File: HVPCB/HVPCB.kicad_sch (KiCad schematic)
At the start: 48 parts, among them U1 NE555DR_C695838, U10 Micro Fit 2P, U2 SN74LVC1GU04DBVR, U3 B0505S-2WR2, U4 LM392MX, U5 AO3400A, U6 AO3400A, U7 KT-0603R, U8 KT-0603R, U9 KT-0603R

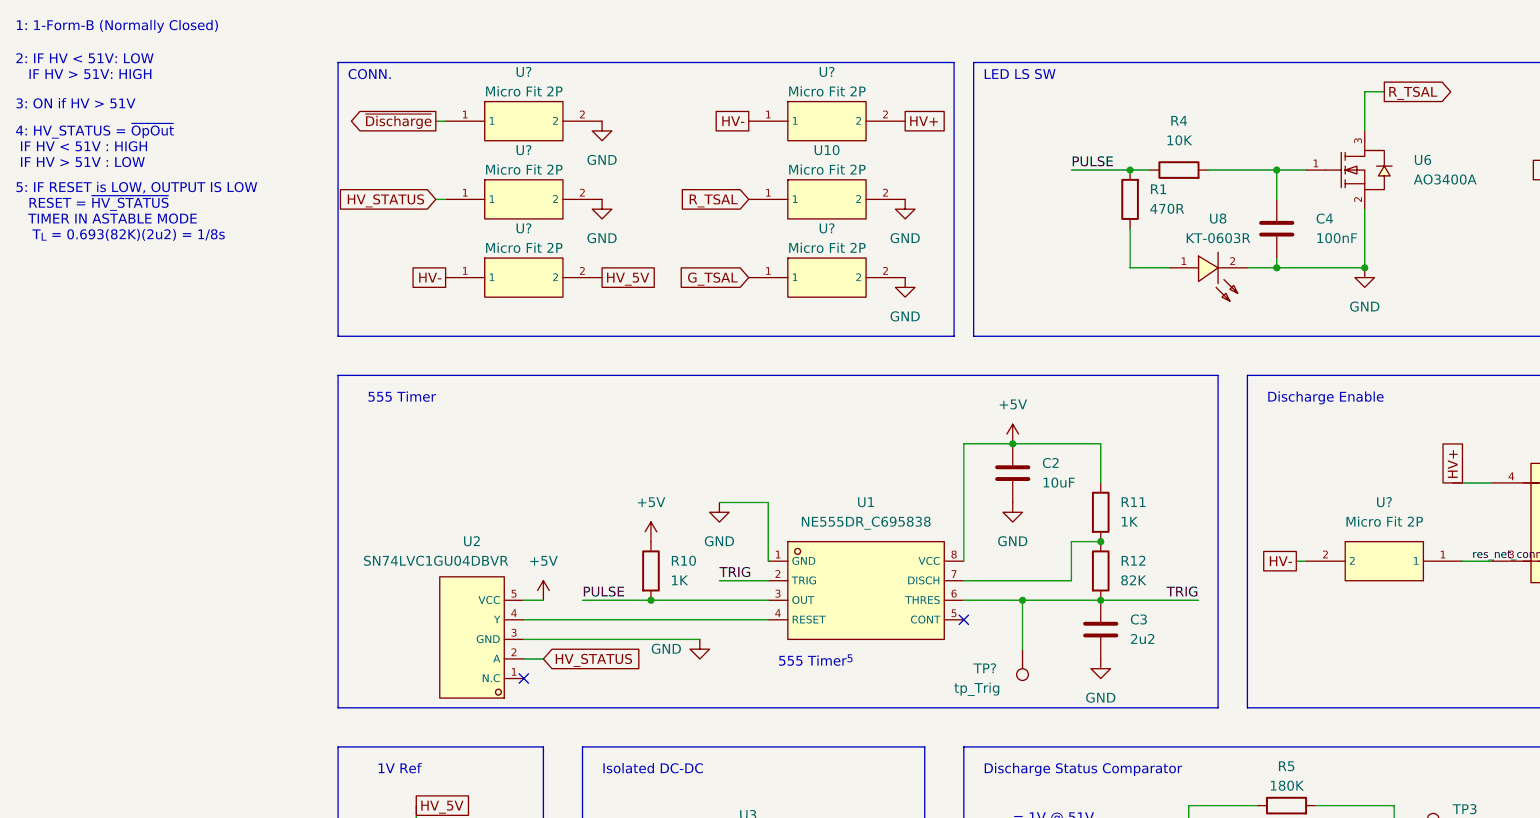
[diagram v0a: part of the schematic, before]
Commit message: updated board drawing to add mounting holes, updated test points and moved components to general proximity
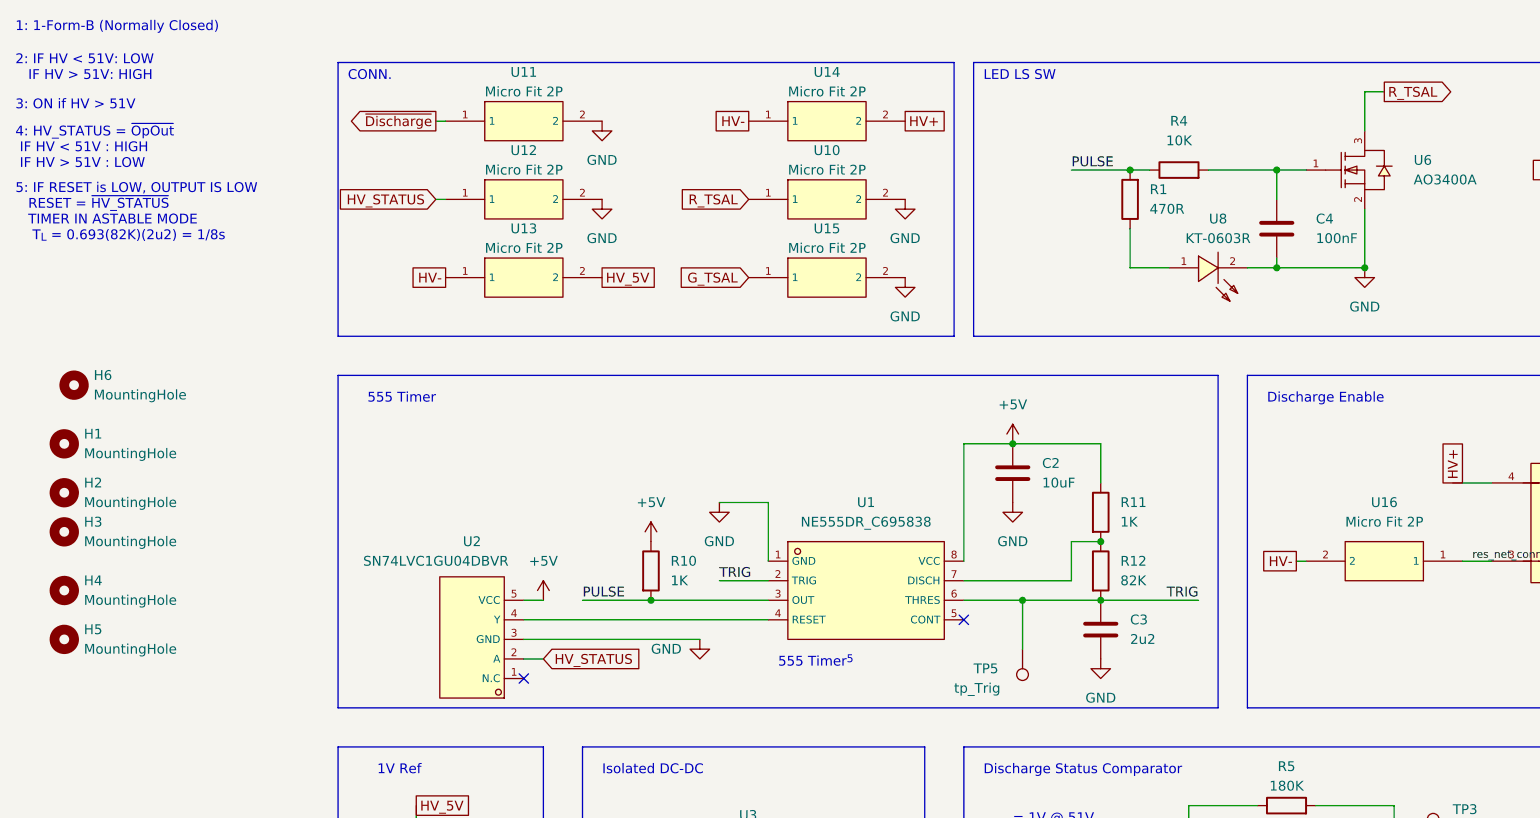
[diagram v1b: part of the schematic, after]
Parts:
- added H1, H2, H3, H4, H5, H6: MountingHole, MountingHole:MountingHole_2.2mm_M2, symbol Mechanical:MountingHole
- TP1: footprint TestPoint:TestPoint_Pad_D2.0mm -> TestPoint:TestPoint_THTPad_D2.0mm_Drill1.0mm
- TP2, TP3, TP4: footprint (none) -> TestPoint:TestPoint_THTPad_D2.0mm_Drill1.0mm
- TP5: renamed from TP?; footprint TestPoint:TestPoint_Pad_D2.0mm -> TestPoint:TestPoint_THTPad_D2.0mm_Drill1.0mm
- gave numbers to parts that had none: 6

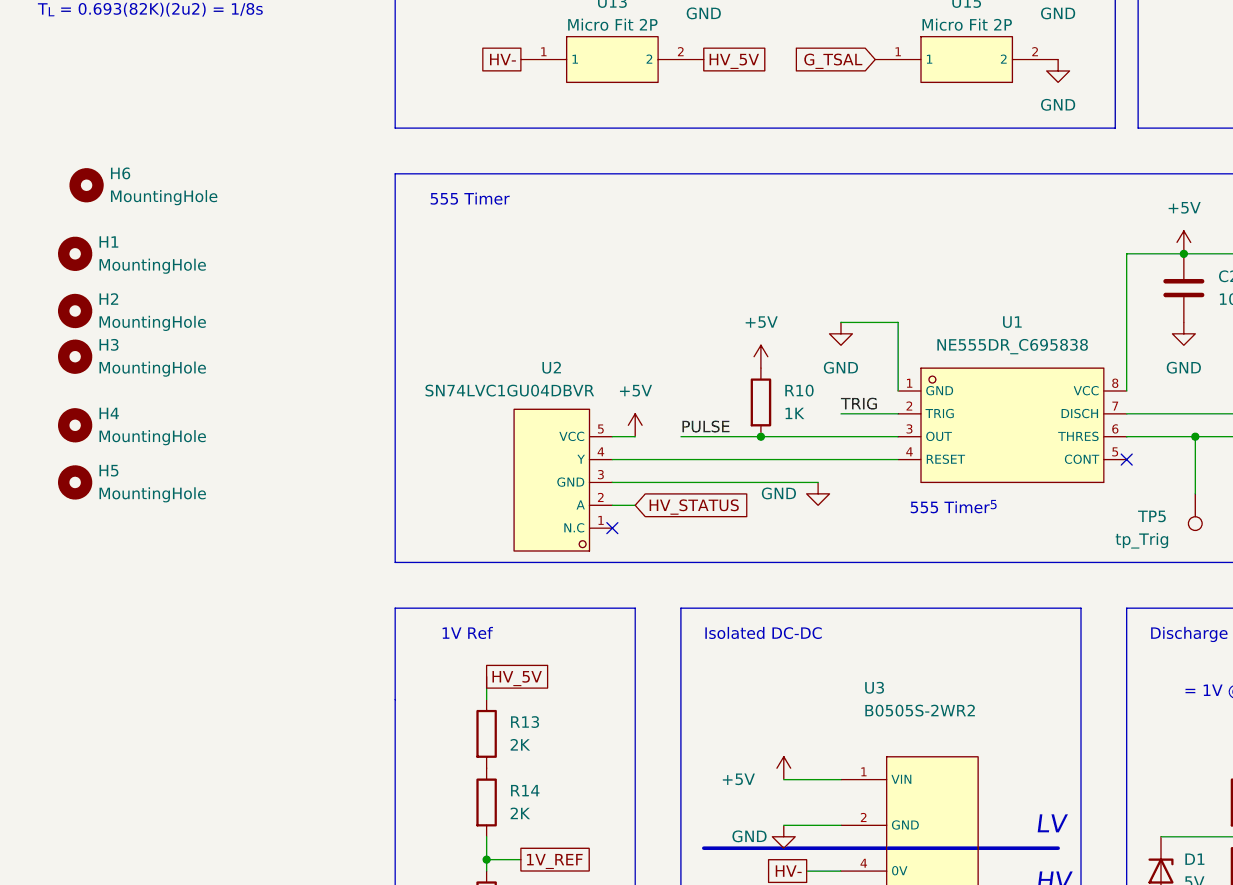
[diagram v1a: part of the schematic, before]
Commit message: added mounting holes and organized board
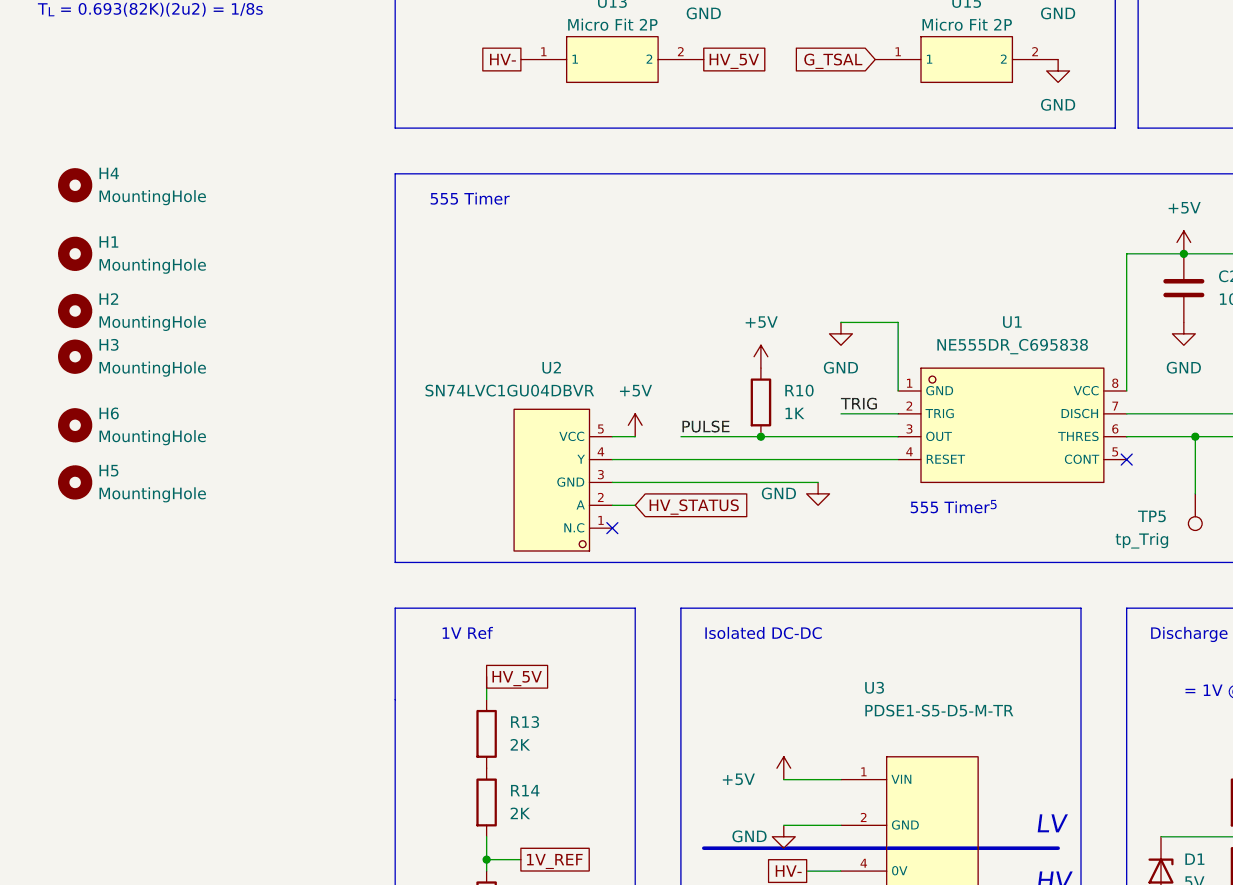
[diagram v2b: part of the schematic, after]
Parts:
- U3: value B0505S-2WR2 -> PDSE1-S5-D5-M-TR; footprint footprint:PWRM-TH_BXXXXS-2WR2 -> Converter_DCDC:CUI Isolated DC-DC; LCSC C41613 -> Mouser; Supplier Link https://www.lcsc.com/product-detail/Power-Modules_B0505S-2W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 -> https://www.mouser.com/ProductDetail/CUI-Inc/PDSE1-S5-D5-M-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
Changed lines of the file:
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@@
     (pin "1")
+  )
+  (symbol (lib_id "Mechanical:MountingHole") (at 22.86 91.44 0) (unit 1)
+    (in_bom yes) (on_board yes) (fields_autoplaced)
+    (property "Reference" "H6" (id 0) (at 25.4 90.1699 0)
+      (effects (font (size 1.27 1.27)) (justify left))
+    )
+    (property "Value" "MountingHole" (id 1) (at 25.4 92.7099 0)
+      (effects (font (size 1.27 1.27)) (justify left))
+    )
+    (property "Footprint" "MountingHole:MountingHole_2.2mm_M2" (id 2) (at 22.86 91.44 0)
+      (effects (font (size 1.27 1.27)) hide)
+    )
+    (property "Datasheet" "~" (id 3) (at 22.86 91.44 0)
+      (effects (font (size 1.27 1.27)) hide)
+    )
   )
   (symbol (lib_id "power:GND") (at 248.92 152.4 0) (unit 1)
@@
     (pin "1")
   )
-  (symbol (lib_id "Mechanical:MountingHole") (at 22.86 91.44 0) (unit 1)
-    (in_bom yes) (on_board yes) (fields_autoplaced)
-    (property "Reference" "H4" (id 0) (at 25.4 90.1699 0)
-      (effects (font (size 1.27 1.27)) (justify left))
-    )
-    (property "Value" "MountingHole" (id 1) (at 25.4 92.7099 0)
-      (effects (font (size 1.27 1.27)) (justify left))
-    )
-    (property "Footprint" "MountingHole:MountingHole_2.2mm_M2" (id 2) (at 22.86 91.44 0)
-      (effects (font (size 1.27 1.27)) hide)
-    )
-    (property "Datasheet" "~" (id 3) (at 22.86 91.44 0)
-      (effects (font (size 1.27 1.27)) hide)
-    )
-  )
   (symbol (lib_id "default_lib:KAQY414S") (at 218.44 80.01 0) (mirror y) (unit 1)
     (in_bom yes) (on_board yes) (fields_autoplaced)
@@
     (pin "1")
     (pin "2")
+  )
+  (symbol (lib_id "Mechanical:MountingHole") (at 22.86 64.77 0) (unit 1)
+    (in_bom yes) (on_board yes) (fields_autoplaced)
+    (property "Reference" "H4" (id 0) (at 25.4 63.4999 0)
+      (effects (font (size 1.27 1.27)) (justify left))
+    )
+    (property "Value" "MountingHole" (id 1) (at 25.4 66.0399 0)
+      (effects (font (size 1.27 1.27)) (justify left))
+    )
+    (property "Footprint" "MountingHole:MountingHole_2.2mm_M2" (id 2) (at 22.86 64.77 0)
+      (effects (font (size 1.27 1.27)) hide)
+    )
+    (property "Datasheet" "~" (id 3) (at 22.86 64.77 0)
+      (effects (font (size 1.27 1.27)) hide)
+    )
   )
   (symbol (lib_id "default_lib:LM392MX") (at 179.07 121.92 0) (unit 1)
@@
       (effects (font (size 1.27 1.27)) (justify left))
     )
-    (property "Value" "B0505S-2WR2" (id 1) (at 110.49 123.19 0)
-      (effects (font (size 1.27 1.27)) (justify left))
-    )
-    (property "Footprint" "footprint:PWRM-TH_BXXXXS-2WR2" (id 2) (at 201.93 200.66 0)
-      (effects (font (size 1.27 1.27) italic) hide)
-    )
-    (property "Datasheet" "https://datasheet.lcsc.com/lcsc/1811131220_MORNSUN-Guangzhou-S--T-B0505S-2WR2_C41613.pdf" (id 3) (at 199.644 190.373 0)
-      (effects (font (size 1.27 1.27)) (justify left) hide)
-    )
-    (property "LCSC" "C41613" (id 4) (at 201.93 190.5 0)
-      (effects (font (size 1.27 1.27)) hide)
-    )
-    (property "Supplier Link" "https://www.lcsc.com/product-detail/Power-Modules_B0505S-2WR2_C41613.html" (id 5) (at 201.93 190.5 0)
+    (property "Value" "PDSE1-S5-D5-M-TR " (id 1) (at 110.49 123.19 0)
+      (effects (font (size 1.27 1.27)) (justify left))
+    )
+    (property "Footprint" "Converter_DCDC:CUI Isolated DC-DC" (id 2) (at 201.93 200.66 0)
+      (effects (font (size 1.27 1.27) italic) hide)
+    )
+    (property "Datasheet" "https://www.mouser.com/datasheet/2/670/pdse1_m-1596038.pdf" (id 3) (at 199.644 190.373 0)
+      (effects (font (size 1.27 1.27)) (justify left) hide)
+    )
+    (property "LCSC" "Mouser" (id 4) (at 201.93 190.5 0)
+      (effects (font (size 1.27 1.27)) hide)
+    )
+    (property "Supplier Link" "https://www.mouser.com/ProductDetail/CUI-Inc/PDSE1-S5-D5-M-TR?qs=T3oQrply3y84xFy4PXEd%252Bg%3D%3D" (id 5) (at 201.93 190.5 0)
       (effects (font (size 1.27 1.27)) hide)
     )
@@
     (pin "1")
     (pin "2")
-  )
-  (symbol (lib_id "Mechanical:MountingHole") (at 24.13 64.77 0) (unit 1)
-    (in_bom yes) (on_board yes) (fields_autoplaced)
-    (property "Reference" "H6" (id 0) (at 26.67 63.4999 0)
-      (effects (font (size 1.27 1.27)) (justify left))
-    )
-    (property "Value" "MountingHole" (id 1) (at 26.67 66.0399 0)
-      (effects (font (size 1.27 1.27)) (justify left))
-    )
-    (property "Footprint" "MountingHole:MountingHole_2.2mm_M2" (id 2) (at 24.13 64.77 0)
-      (effects (font (size 1.27 1.27)) hide)
-    )
-    (property "Datasheet" "~" (id 3) (at 24.13 64.77 0)
-      (effects (font (size 1.27 1.27)) hide)
-    )
   )
   (symbol (lib_id "Device:R") (at 157.48 88.9 0) (unit 1)
@@
       (reference "H3") (unit 1) (value "MountingHole") (footprint "MountingHole:MountingHole_2.2mm_M2")
     )
-    (path "/2dac9e5a-0655-46d9-a99c-048a20f87a89"
+    (path "/914ef98e-a36e-4b71-97d8-24673dfd0278"
       (reference "H4") (unit 1) (value "MountingHole") (footprint "MountingHole:MountingHole_2.2mm_M2")
     )
@@
       (reference "H5") (unit 1) (value "MountingHole") (footprint "MountingHole:MountingHole_2.2mm_M2")
     )
-    (path "/c6a8c9f2-61de-4a32-9bc7-20b27a842778"
+    (path "/18c58822-4a31-4b97-b45e-eb2dbef7de2d"
       (reference "H6") (unit 1) (value "MountingHole") (footprint "MountingHole:MountingHole_2.2mm_M2")
     )
@@
     )
     (path "/c46c3c89-699d-4877-8550-c3868031a0da"
-      (reference "U3") (unit 1) (value "B0505S-2WR2") (footprint "footprint:PWRM-TH_BXXXXS-2WR2")
+      (reference "U3") (unit 1) (value "PDSE1-S5-D5-M-TR ") (footprint "Converter_DCDC:CUI Isolated DC-DC")
     )
     (path "/94cf2218-519f-4374-9cb9-5e02f8aa7660"

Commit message: layout almost done
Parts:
- removed U10, U11, U12, U13, U15: Micro Fit 2P, footprint:CONN-TH_43045-0200, symbol default_lib:0430450200
- added J1: Micro Fit 10p, Connector_Molex:Molex_Micro-Fit_3.0_43650-1010_1x10-1MP_P3.00mm_Horizontal, symbol Connector:Conn_01x10_Female
- added Q1: OnSemi FDB12N50TM, Package_TO_SOT_SMD:TO-263-2_TabPin1_D2PAK, symbol Transistor_FET:BS170
- added R8, R9: 1K, Resistor_SMD:R_0603_1608Metric_Pad0.98x0.95mm_HandSolder, symbol Device:R
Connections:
- net +5V: now also J1.4 (Pin_4)
- net GND: now also J1.1 (Pin_1), J1.10 (Pin_10), J1.3 (Pin_3), J1.5 (Pin_5), J1.8 (Pin_8)
- net G_TSAL: now also J1.7 (Pin_7)
- net HV+: now also Q1.1 (D); no longer S1.4
- net HV-: now also U16.1, R8.1; no longer U16.2
- net HV_5V: now also S1.4, U3.5 (+Vo); no longer U3.6 (+Vo)
- net HV_STATUS: now also J1.9 (Pin_9)
- net R_TSAL: now also J1.6 (Pin_6)
- net res_net_conn: no longer S1.3, U16.1
- net ~{Discharge}: now also J1.2 (Pin_2)
- new net: R9.1, S1.3
- new net: Q1.2 (G), R8.2, R9.2
- new net: Q1.3 (S), U16.2
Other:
- moved on the sheet: U14, U16

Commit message: finished layout
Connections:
- net HV+: now also U14.1; no longer U14.2
- net HV-: now also U14.2, U16.2; no longer U14.1, U16.1
- net at Q1.3 (S): now also U16.1; no longer U16.2
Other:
- moved on the sheet: U16
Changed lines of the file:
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@@
     )
   )
-  (global_label "HV+" (shape passive) (at 128.27 39.37 0) (fields_autoplaced)
+  (global_label "HV+" (shape passive) (at 107.95 39.37 180) (fields_autoplaced)
+    (effects (font (size 1.27 1.27)) (justify right))
+    (property "Intersheet References" "${INTERSHEET_REFS}" (id 0) (at 101.5455 39.4494 0)
+      (effects (font (size 1.27 1.27)) (justify right) hide)
+    )
+  )
+  (global_label "R_TSAL" (shape output) (at 194.31 26.67 0) (fields_autoplaced)
+    (effects (font (size 1.27 1.27)) (justify left))
+    (property "Intersheet References" "${INTERSHEET_REFS}" (id 0) (at 203.2545 26.5906 0)
+      (effects (font (size 1.27 1.27)) (justify left) hide)
+    )
+  )
+  (global_label "HV+" (shape passive) (at 191.77 82.55 90) (fields_autoplaced)
+    (effects (font (size 1.27 1.27)) (justify left))
+    (property "Intersheet References" "${INTERSHEET_REFS}" (id 0) (at 191.6906 76.1455 90)
+      (effects (font (size 1.27 1.27)) (justify left) hide)
+    )
+  )
+  (global_label "HV-" (shape passive) (at 128.27 39.37 0) (fields_autoplaced)
     (effects (font (size 1.27 1.27)) (justify left))
     (property "Intersheet References" "${INTERSHEET_REFS}" (id 0) (at 134.6745 39.2906 0)
       (effects (font (size 1.27 1.27)) (justify left) hide)
-    )
-  )
-  (global_label "R_TSAL" (shape output) (at 194.31 26.67 0) (fields_autoplaced)
-    (effects (font (size 1.27 1.27)) (justify left))
-    (property "Intersheet References" "${INTERSHEET_REFS}" (id 0) (at 203.2545 26.5906 0)
-      (effects (font (size 1.27 1.27)) (justify left) hide)
-    )
-  )
-  (global_label "HV+" (shape passive) (at 191.77 82.55 90) (fields_autoplaced)
-    (effects (font (size 1.27 1.27)) (justify left))
-    (property "Intersheet References" "${INTERSHEET_REFS}" (id 0) (at 191.6906 76.1455 90)
-      (effects (font (size 1.27 1.27)) (justify left) hide)
-    )
-  )
-  (global_label "HV-" (shape passive) (at 107.95 39.37 180) (fields_autoplaced)
-    (effects (font (size 1.27 1.27)) (justify right))
-    (property "Intersheet References" "${INTERSHEET_REFS}" (id 0) (at 101.5455 39.4494 0)
-      (effects (font (size 1.27 1.27)) (justify right) hide)
     )
   )
@@
     (pin "1")
   )
-  (symbol (lib_id "default_lib:0430450200") (at 196.85 82.55 270) (unit 1)
+  (symbol (lib_id "default_lib:0430450200") (at 171.45 82.55 90) (unit 1)
     (in_bom yes) (on_board yes)
-    (property "Reference" "U16" (id 0) (at 186.69 73.66 90)
-      (effects (font (size 1.27 1.27)) (justify left))
-    )
-    (property "Value" "Micro Fit 2P" (id 1) (at 186.69 76.2 90)
-      (effects (font (size 1.27 1.27)) (justify left))
-    )
-    (property "Footprint" "footprint:CONN-TH_43045-0200" (id 2) (at 186.69 82.55 0)
+    (property "Reference" "U16" (id 0) (at 181.61 91.44 90)
+      (effects (font (size 1.27 1.27)) (justify left))
+    )
+    (property "Value" "Micro Fit 2P" (id 1) (at 181.61 88.9 90)
+      (effects (font (size 1.27 1.27)) (justify left))
+    )
+    (property "Footprint" "footprint:CONN-TH_43045-0200" (id 2) (at 181.61 82.55 0)
       (effects (font (size 1.27 1.27) italic) hide)
     )
-    (property "Datasheet" "https://datasheet.lcsc.com/lcsc/1811051320_MOLEX-430450200_C122431.pdf" (id 3) (at 196.977 80.264 0)
-      (effects (font (size 1.27 1.27)) (justify left) hide)
-    )
-    (property "LCSC" "C122431" (id 4) (at 196.85 82.55 0)
-      (effects (font (size 1.27 1.27)) hide)
-    )
+    (property "Datasheet" "https://datasheet.lcsc.com/lcsc/1811051320_MOLEX-430450200_C122431.pdf" (id 3) (at 171.323 84.836 0)
+      (effects (font (size 1.27 1.27)) (justify left) hide)
+    )
+    (property "LCSC" "C122431" (id 4) (at 171.45 82.55 0)
+      (effects (font (size 1.27 1.27)) hide)
+    )
